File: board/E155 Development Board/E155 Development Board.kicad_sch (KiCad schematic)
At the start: 46 parts, among them J1 Screw_Terminal_01x02, J2 Conn_01x03, J3 Conn_01x02, J4 Conn_01x02, J6 Conn_02x20_Odd_Even, J7 Conn_01x06, SW0 SW_Push, SW1 SW_Push, SW2 SW_Push, SW3 SW_Push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

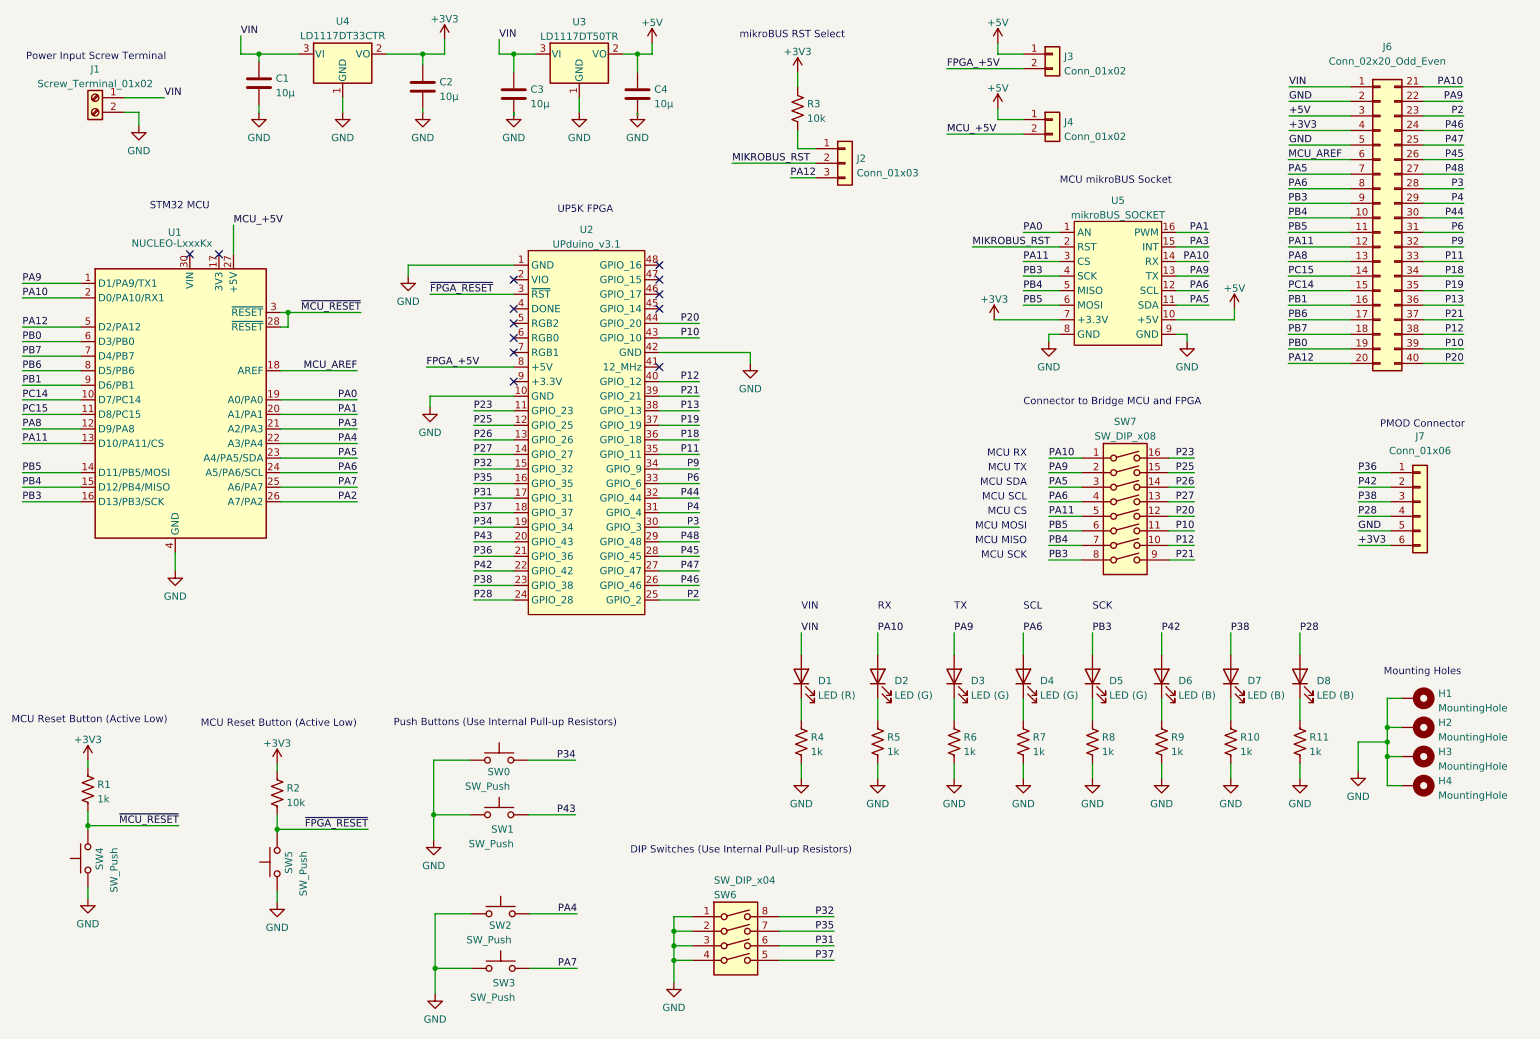
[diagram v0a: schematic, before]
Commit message: Board updates for FA24
Removed specific text on the board which references a year and changed it to a version number. Also updated the libraries and KiCad files to resolve design check issues.
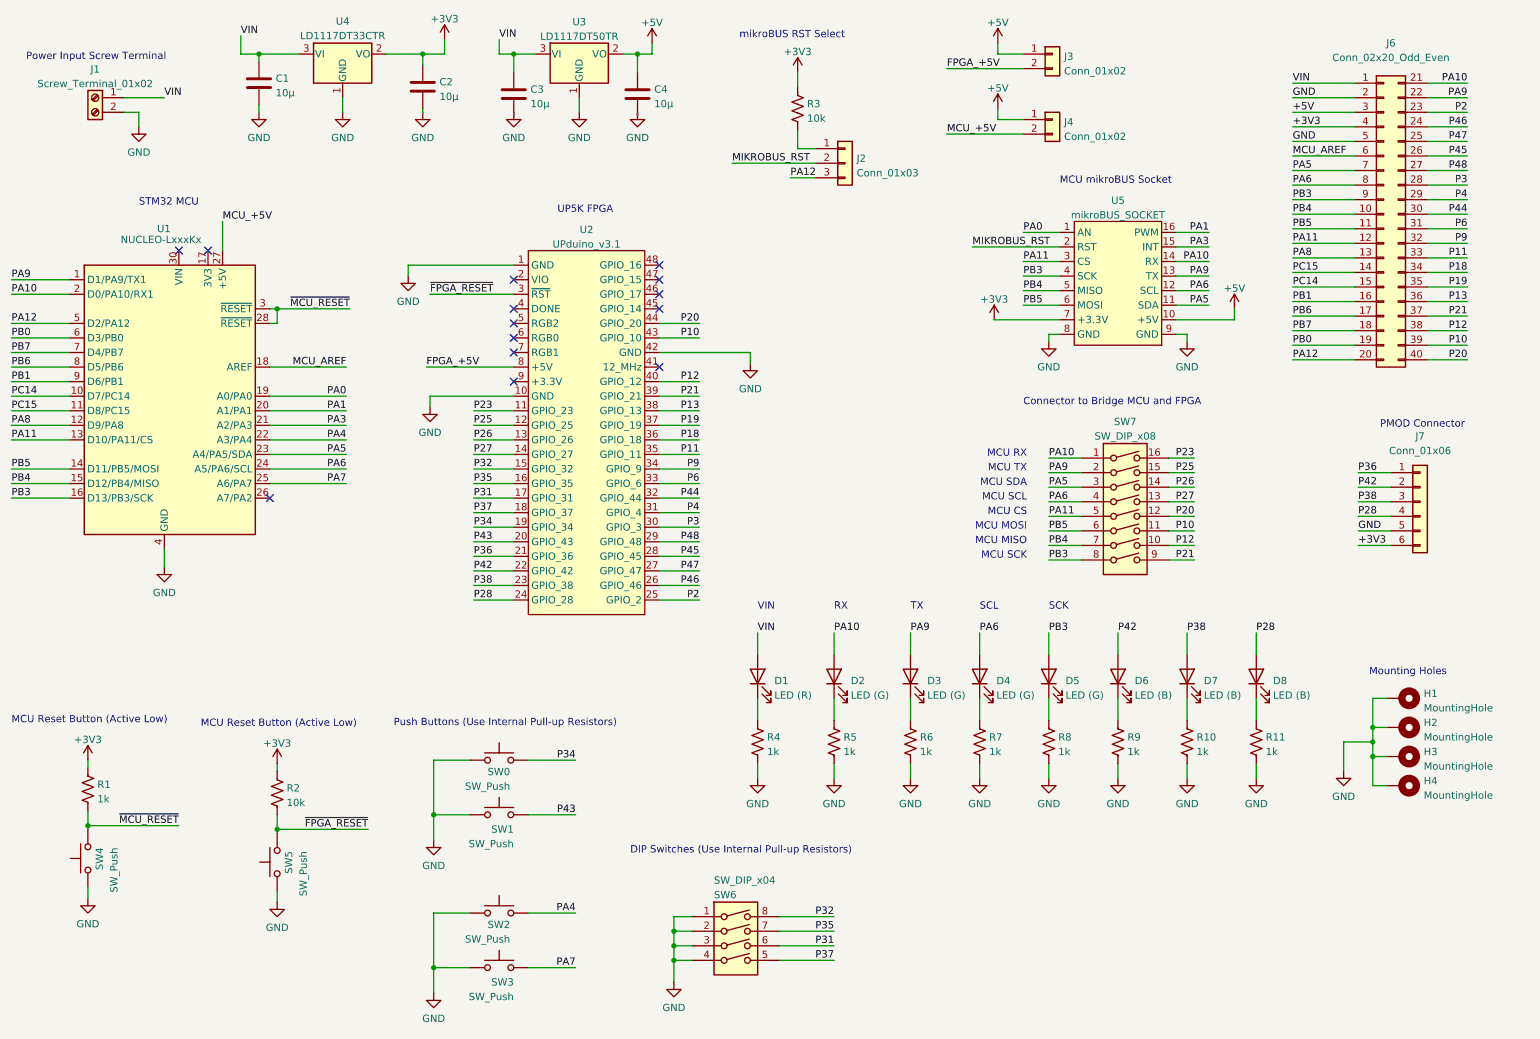
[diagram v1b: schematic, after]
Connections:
- net PA2: no longer names the net of U1.26 (A7/PA2)
- no-connect marks 13 -> 14
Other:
- title: E155 FA23 Development Board -> E155 Development Board
- moved on the sheet: D1, D2, D3, D4, D5, D6, D7, D8, H1, H2, H3, H4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
